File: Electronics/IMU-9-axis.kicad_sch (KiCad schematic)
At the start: 4 parts, among them U1 ICM-20948

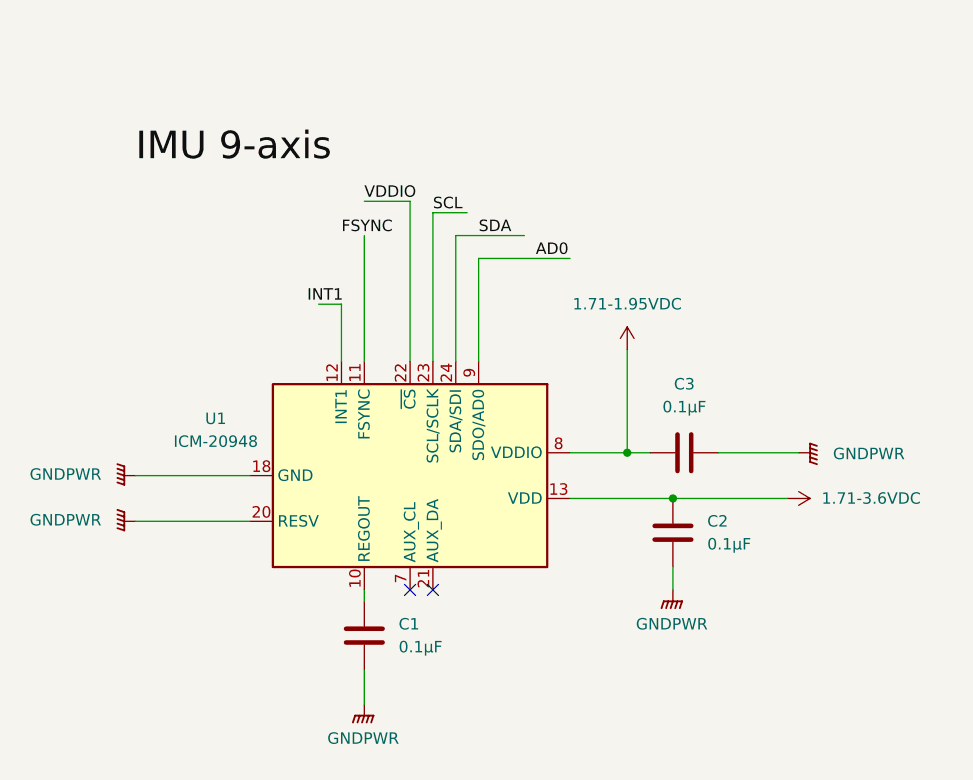
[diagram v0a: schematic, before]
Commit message: 9-axis IMU corrected schematics
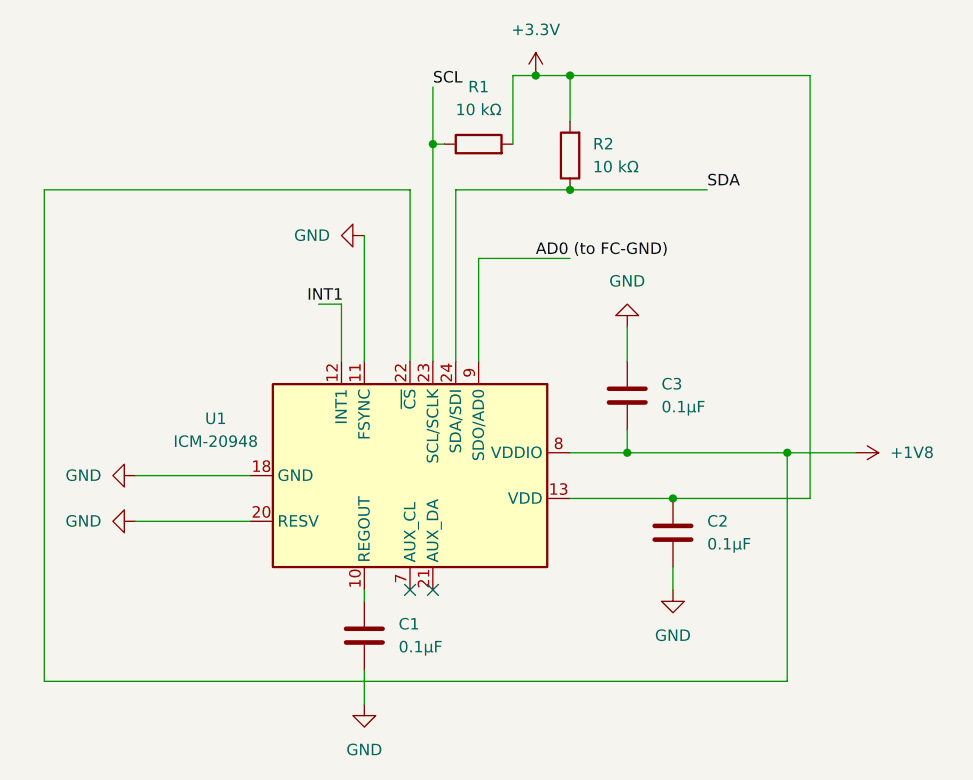
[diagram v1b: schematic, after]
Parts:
- added R1, R2: 10 kΩ, symbol Device:R
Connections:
- net VDDIO is gone; now on net +1V8: U1.22 (~{CS})
- net SCL: now also R1.1
- net SDA: now also R2.1
- net GND: now reaches U1.11 (FSYNC)
- net GND: now also C1.2, C2.2, C3.2, U1.18 (GND), U1.20 (RESV)
- net 1.71-1.95VDC renamed +1V8
- net +1V8: now also C3.1; no longer C3.2
- net 1.71-3.6VDC renamed +3.3V
- net +3.3V: now also R1.2, R2.2
- net AD0 renamed AD0 (to FC-GND)
- removed net GNDPWR: C1.2, C2.2, C3.1, U1.18 (GND), U1.20 (RESV)
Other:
- moved on the sheet: C3

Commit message: filing details added to 9-axis IMU
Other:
- company: (none) -> Propulsive Landers @ GT
- title: (none) -> ICM 20948 (9-axis IMU) Board
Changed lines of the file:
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@@
 	(generator_version "8.0")
 	(paper "A4")
+	(title_block
+		(title "ICM 20948 (9-axis IMU) Board")
+		(date "2024-10-01")
+		(rev "1")
+		(company "Propulsive Landers @ GT")
+		(comment 1 "GND = Analog Ground (no digital ground here)")
+	)
 	(junction
 		(at 82.55 43.18)
